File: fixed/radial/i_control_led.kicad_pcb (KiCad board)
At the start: 2 copper layers, 25.4 x 20 mm, 18 parts, among them J1 Conn_01x04, J2 Conn_01x04, M1 MountingHole_2.5mm_Pad, M2 MountingHole_2.5mm_Pad, M3 MountingHole_2.5mm_Pad, M4 MountingHole_2.5mm_Pad, Q1 MMBT5551L, U1 LM2775DSG, U2 LMV321

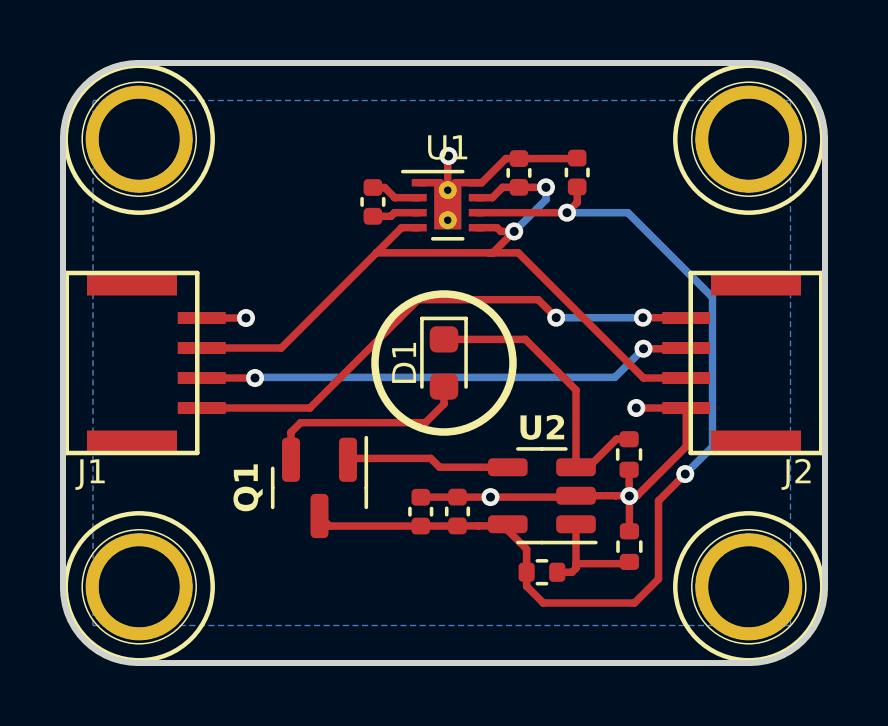
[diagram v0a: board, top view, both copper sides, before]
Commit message: Added fixed current radial led design.
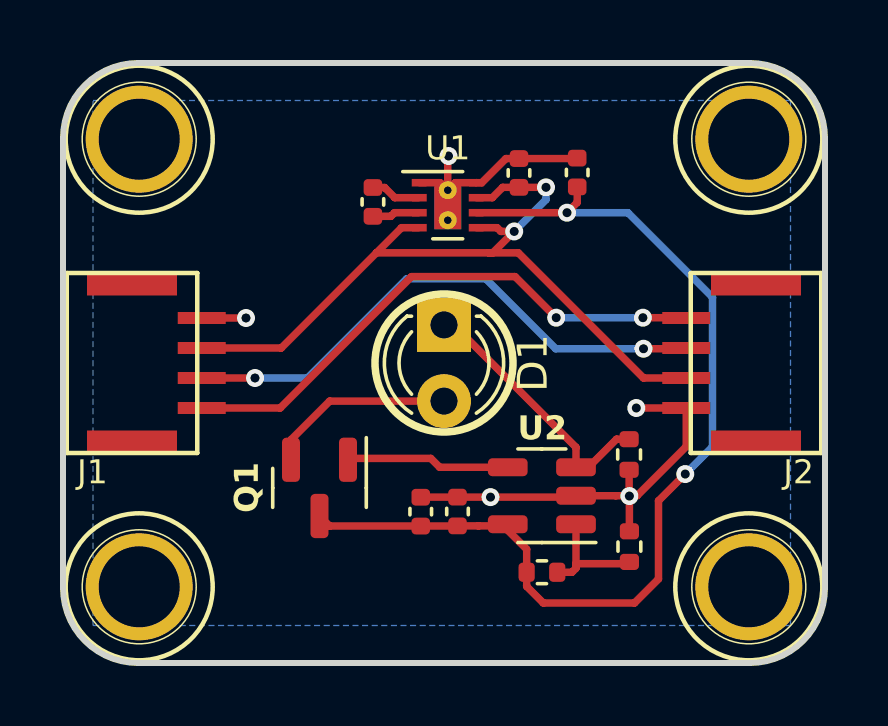
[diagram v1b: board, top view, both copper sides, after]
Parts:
- D1: footprint LED_SMD:LED_0603_1608Metric -> LED_THT:LED_D3.0mm
- R2: value 18k -> 10k
- moved D1 1.27 mm to (62.7, 58.7)
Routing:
- net /SDA: track 16.6 -> 18.5 mm
- net Net-(D1-K): track 9.83 -> 8.91 mm
- net Net-(D1-A): track 6.99 -> 6.30 mm
- net /SCL: track 17.9 -> 18.5 mm
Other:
- board text added: "IControl LED V0.1 R1 www.iorodeo.com white, I=25mA Vin=3.3-5V"
- board text removed: "IControl LED V0.1 R1 www.iorodeo.com white, I=18mA Vin=3.3-5V"
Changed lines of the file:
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@@
     (pad "~" thru_hole circle (at 0 0) (size 3.57 3.57) (drill 2.7) (layers "*.Cu" "*.Mask"))
   )
-  (footprint "LED_SMD:LED_0603_1608Metric" (layer "F.Cu")
-    (at 62.7 60 -90)
-    (descr "LED SMD 0603 (1608 Metric), square (rectangular) end terminal, IPC_7351 nominal, (Body size source: http://www.tortai-tech.com/upload/download/2011102023233369053.pdf), generated with kicad-footprint-generator")
-    (tags "LED")
-    (property "Sheetfile" "i_control_led.kicad_sch")
-    (property "Sheetname" "")
-    (attr smd)
-    (fp_text reference "D1" (at 0 1.3 270) (layer "F.SilkS")
-        (effects (font (size 0.8 0.8) (thickness 0.16)))
-    )
-    (fp_text value "LED_ALT" (at 0 1.43 90) (layer "F.Fab") hide
-        (effects (font (size 1 1) (thickness 0.15)))
-    )
-    (fp_text user "${REFERENCE}" (at 0 0 90) (layer "F.Fab")
-        (effects (font (size 0.8 0.8) (thickness 0.16)))
-    )
-    (fp_line (start -1.485 -0.735) (end -1.485 0.735)
-      (stroke (width 0.12) (type solid)) (layer "F.SilkS"))
-    (fp_line (start -1.485 0.735) (end 0.8 0.735)
-      (stroke (width 0.12) (type solid)) (layer "F.SilkS"))
-    (fp_line (start 0.8 -0.735) (end -1.485 -0.735)
-      (stroke (width 0.12) (type solid)) (layer "F.SilkS"))
-    (fp_line (start -1.48 -0.73) (end 1.48 -0.73)
-      (stroke (width 0.05) (type solid)) (layer "F.CrtYd"))
-    (fp_line (start -1.48 0.73) (end -1.48 -0.73)
-      (stroke (width 0.05) (type solid)) (layer "F.CrtYd"))
-    (fp_line (start 1.48 -0.73) (end 1.48 0.73)
-      (stroke (width 0.05) (type solid)) (layer "F.CrtYd"))
-    (fp_line (start 1.48 0.73) (end -1.48 0.73)
-      (stroke (width 0.05) (type solid)) (layer "F.CrtYd"))
-    (fp_line (start -0.8 -0.1) (end -0.8 0.4)
-      (stroke (width 0.1) (type solid)) (layer "F.Fab"))
-    (fp_line (start -0.8 0.4) (end 0.8 0.4)
-      (stroke (width 0.1) (type solid)) (layer "F.Fab"))
-    (fp_line (start -0.5 -0.4) (end -0.8 -0.1)
-      (stroke (width 0.1) (type solid)) (layer "F.Fab"))
-    (fp_line (start 0.8 -0.4) (end -0.5 -0.4)
-      (stroke (width 0.1) (type solid)) (layer "F.Fab"))
-    (fp_line (start 0.8 0.4) (end 0.8 -0.4)
-      (stroke (width 0.1) (type solid)) (layer "F.Fab"))
-    (pad "1" smd roundrect (at -0.7875 0 270) (size 0.875 0.95) (layers "F.Cu" "F.Paste" "F.Mask") (roundrect_rratio 0.25)
+  (footprint "LED_THT:LED_D3.0mm" (layer "F.Cu")
+    (at 62.7 58.73 -90)
+    (descr "LED, diameter 3.0mm, 2 pins")
+    (tags "LED diameter 3.0mm 2 pins")
+    (property "Sheetfile" "i_control_led.kicad_sch")
+    (property "Sheetname" "")
+    (attr through_hole)
+    (fp_text reference "D1" (at 1.27 -2.96 90) (layer "F.SilkS")
+        (effects (font (size 1 1) (thickness 0.15)))
+    )
+    (fp_text value "LED_ALT" (at 1.27 2.96 90) (layer "F.Fab")
+        (effects (font (size 1 1) (thickness 0.15)))
+    )
+    (fp_line (start -0.29 -1.236) (end -0.29 -1.08)
+      (stroke (width 0.12) (type solid)) (layer "F.SilkS"))
+    (fp_line (start -0.29 1.08) (end -0.29 1.236)
+      (stroke (width 0.12) (type solid)) (layer "F.SilkS"))
+    (fp_arc (start -0.29 -1.235516) (mid 1.366487 -1.987659) (end 2.942335 -1.078608)
+      (stroke (width 0.12) (type solid)) (layer "F.SilkS"))
+    (fp_arc (start 0.229039 -1.08) (mid 1.270117 -1.5) (end 2.31113 -1.079837)
+      (stroke (width 0.12) (type solid)) (layer "F.SilkS"))
+    (fp_arc (start 2.31113 1.079837) (mid 1.270117 1.5) (end 0.229039 1.08)
+      (stroke (width 0.12) (type solid)) (layer "F.SilkS"))
+    (fp_arc (start 2.942335 1.078608) (mid 1.366487 1.987659) (end -0.29 1.235516)
+      (stroke (width 0.12) (type solid)) (layer "F.SilkS"))
+    (fp_line (start -1.15 -2.25) (end -1.15 2.25)
+      (stroke (width 0.05) (type solid)) (layer "F.CrtYd"))
+    (fp_line (start -1.15 2.25) (end 3.7 2.25)
+      (stroke (width 0.05) (type solid)) (layer "F.CrtYd"))
+    (fp_line (start 3.7 -2.25) (end -1.15 -2.25)
+      (stroke (width 0.05) (type solid)) (layer "F.CrtYd"))
+    (fp_line (start 3.7 2.25) (end 3.7 -2.25)
+      (stroke (width 0.05) (type solid)) (layer "F.CrtYd"))
+    (fp_line (start -0.23 -1.16619) (end -0.23 1.16619)
+      (stroke (width 0.1) (type solid)) (layer "F.Fab"))
+    (fp_arc (start -0.23 -1.16619) (mid 3.17 0.000452) (end -0.230555 1.165476)
+      (stroke (width 0.1) (type solid)) (layer "F.Fab"))
+    (fp_circle (center 1.27 0) (end 2.77 0)
+      (stroke (width 0.1) (type solid)) (fill none) (layer "F.Fab"))
+    (pad "1" thru_hole rect (at 0 0 270) (size 1.8 1.8) (drill 0.9) (layers "*.Cu" "*.Mask")
       (net 8 "Net-(D1-K)") (pinfunction "K") (pintype "passive"))
-    (pad "2" smd roundrect (at 0.7875 0 270) (size 0.875 0.95) (layers "F.Cu" "F.Paste" "F.Mask") (roundrect_rratio 0.25)
+    (pad "2" thru_hole circle (at 2.54 0 270) (size 1.8 1.8) (drill 0.9) (layers "*.Cu" "*.Mask")
       (net 9 "Net-(D1-A)") (pinfunction "A") (pintype "passive"))
-    (model "${KISYS3DMOD}/LED_SMD.3dshapes/LED_0603_1608Metric.wrl"
+    (model "${KICAD6_3DMODEL_DIR}/LED_THT.3dshapes/LED_D3.0mm.wrl"
       (offset (xyz 0 0 0))
       (scale (xyz 1 1 1))
@@
         (effects (font (size 1 1) (thickness 0.15)))
     )
-    (fp_text value "18k" (at 0 1.17) (layer "F.Fab") hide
+    (fp_text value "10k" (at 0 1.17) (layer "F.Fab") hide
         (effects (font (size 1 1) (thickness 0.15)))
     )
@@
   (gr_line (start 75.4 52.5) (end 75.4 67.5)
     (stroke (width 0.2) (type solid)) (layer "Edge.Cuts"))
-  (gr_text "IControl LED V0.1 R1\nwww.iorodeo.com\nwhite, I=18mA\nVin=3.3-5V" (at 62.7 60) (layer "B.SilkS")
+  (gr_text "IControl LED V0.1 R1\nwww.iorodeo.com\nwhite, I=25mA\nVin=3.3-5V" (at 62.7 60) (layer "B.SilkS")
     (effects (font (size 1 1) (thickness 0.15)) (justify mirror))
   )
@@
   (segment (start 61.05 54.99) (end 61.875 54.99) (width 0.25) (layer "F.Cu") (net 3))
   (segment (start 60.93 55.11) (end 61.05 54.99) (width 0.25) (layer "F.Cu") (net 3))
-  (segment (start 65.84 57.89) (end 61.84 57.89) (width 0.25) (layer "F.Cu") (net 4))
-  (segment (start 58.23 61.5) (end 54.625 61.5) (width 0.25) (layer "F.Cu") (net 4))
+  (segment (start 57.24 61.5) (end 54.625 61.5) (width 0.25) (layer "F.Cu") (net 4))
+  (segment (start 61.62 57.12) (end 57.24 61.5) (width 0.25) (layer "F.Cu") (net 4))
+  (segment (start 66.44 58.49) (end 65.07 57.12) (width 0.25) (layer "F.Cu") (net 4))
+  (segment (start 65.07 57.12) (end 61.62 57.12) (width 0.25) (layer "F.Cu") (net 4))
   (segment (start 69.33 58.49) (end 70.765 58.49) (width 0.25) (layer "F.Cu") (net 4))
-  (segment (start 66.44 58.49) (end 65.84 57.89) (width 0.25) (layer "F.Cu") (net 4))
-  (segment (start 61.84 57.89) (end 58.23 61.5) (width 0.25) (layer "F.Cu") (net 4))
   (via (at 69.33 58.49) (size 0.6) (drill 0.3) (layers "F.Cu" "B.Cu") (net 4))
   (via (at 66.44 58.49) (size 0.6) (drill 0.3) (layers "F.Cu" "B.Cu") (net 4))
@@
   (via (at 56.4 60.5) (size 0.6) (drill 0.3) (layers "F.Cu" "B.Cu") (net 5))
   (via (at 69.35 59.525) (size 0.6) (drill 0.3) (layers "F.Cu" "B.Cu") (net 5))
-  (segment (start 56.42 60.48) (end 68.395 60.48) (width 0.25) (layer "B.Cu") (net 5))
-  (segment (start 56.4 60.5) (end 56.42 60.48) (width 0.25) (layer "B.Cu") (net 5))
-  (segment (start 68.395 60.48) (end 69.35 59.525) (width 0.25) (layer "B.Cu") (net 5))
+  (segment (start 61.46 57.19) (end 64.11 57.19) (width 0.25) (layer "B.Cu") (net 5))
+  (segment (start 56.4 60.5) (end 58.15 60.5) (width 0.25) (layer "B.Cu") (net 5))
+  (segment (start 66.425 59.525) (end 69.35 59.525) (width 0.25) (layer "B.Cu") (net 5))
+  (segment (start 58.15 60.5) (end 61.46 57.19) (width 0.25) (layer "B.Cu") (net 5))
+  (segment (start 64.11 57.21) (end 66.425 59.525) (width 0.25) (layer "B.Cu") (net 5))
+  (segment (start 64.11 57.19) (end 64.11 57.21) (width 0.25) (layer "B.Cu") (net 5))
   (segment (start 60.72 54.15) (end 61.06 54.49) (width 0.25) (layer "F.Cu") (net 6))
   (segment (start 60.33 54.15) (end 60.72 54.15) (width 0.25) (layer "F.Cu") (net 6))
@@
   (segment (start 71.65 62.793178) (end 71.65 57.81) (width 0.25) (layer "B.Cu") (net 7))
   (segment (start 68.45 62.54) (end 68.87 62.54) (width 0.25) (layer "F.Cu") (net 8))
-  (segment (start 65.4125 59.2125) (end 67.1 60.9) (width 0.25) (layer "F.Cu") (net 8))
-  (segment (start 67.1 60.9) (end 67.1 63.475) (width 0.25) (layer "F.Cu") (net 8))
-  (segment (start 62.7 59.2125) (end 65.4125 59.2125) (width 0.25) (layer "F.Cu") (net 8))
+  (segment (start 67.1 62.81) (end 67.1 63.475) (width 0.25) (layer "F.Cu") (net 8))
+  (segment (start 62.7 58.73) (end 63.02 58.73) (width 0.25) (layer "F.Cu") (net 8))
+  (segment (start 63.02 58.73) (end 67.1 62.81) (width 0.25) (layer "F.Cu") (net 8))
   (segment (start 67.515 63.475) (end 68.45 62.54) (width 0.25) (layer "F.Cu") (net 8))
   (segment (start 67.1 63.475) (end 67.515 63.475) (width 0.25) (layer "F.Cu") (net 8))
-  (segment (start 62.08 61.99) (end 57.92 61.99) (width 0.25) (layer "F.Cu") (net 9))
-  (segment (start 57.6 62.31) (end 57.6 63.225) (width 0.25) (layer "F.Cu") (net 9))
-  (segment (start 57.92 61.99) (end 57.6 62.31) (width 0.25) (layer "F.Cu") (net 9))
-  (segment (start 62.7 60.7875) (end 62.7 61.37) (width 0.25) (layer "F.Cu") (net 9))
-  (segment (start 62.7 61.37) (end 62.08 61.99) (width 0.25) (layer "F.Cu") (net 9))
+  (segment (start 57.6 62.56) (end 58.89 61.27) (width 0.25) (layer "F.Cu") (net 9))
+  (segment (start 57.6 63.225) (end 57.6 62.56) (width 0.25) (layer "F.Cu") (net 9))
+  (segment (start 58.89 61.27) (end 62.7 61.27) (width 0.25) (layer "F.Cu") (net 9))
   (segment (start 64.825 63.475) (end 62.555 63.475) (width 0.25) (layer "F.Cu") (net 10))
   (segment (start 59.545 63.18) (end 59.5 63.225) (width 0.25) (layer "F.Cu") (net 10))
